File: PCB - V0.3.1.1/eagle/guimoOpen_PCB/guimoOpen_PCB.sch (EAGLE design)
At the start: 8 parts, among them M1 ARDUINO-NANO-3.0, U1 GY-521MPU6050

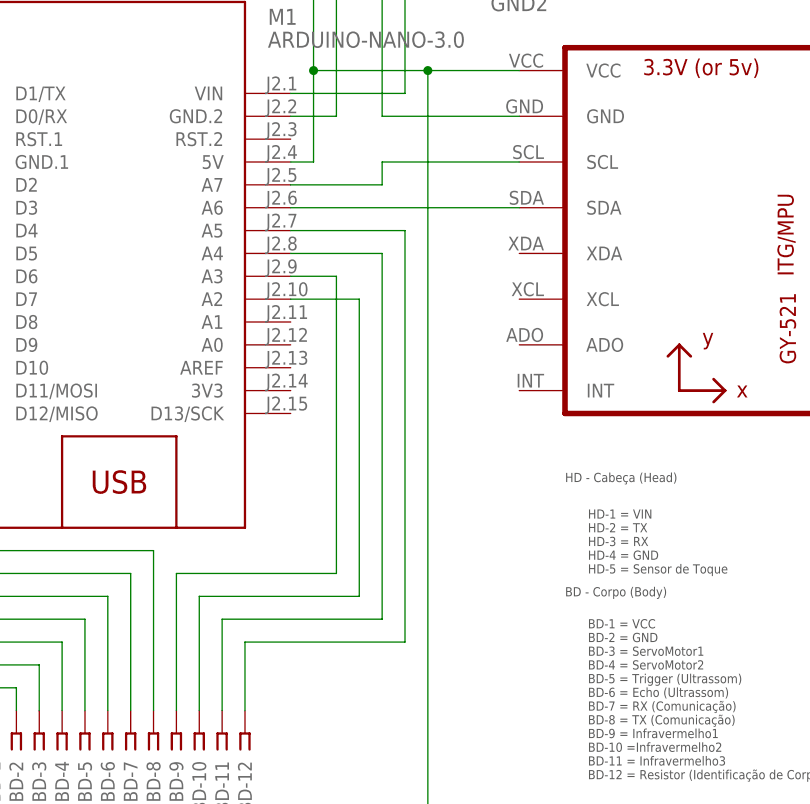
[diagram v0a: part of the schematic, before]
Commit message: Correção do roteamento do acelerômetro. SDA e SCL foram colocadas nas portas A4 e A5
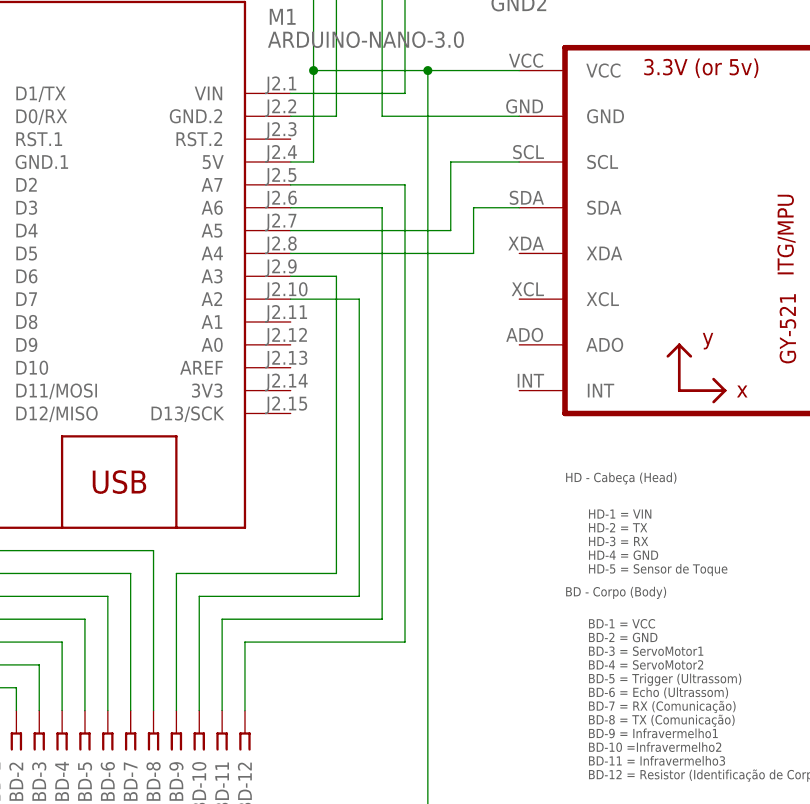
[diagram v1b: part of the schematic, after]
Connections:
- net N$15: now also M1.A7; no longer M1.A5
- net N$16: now also M1.A6; no longer M1.A4
- net N$3: now also M1.A5; no longer M1.A7
- net N$4: now also M1.A4; no longer M1.A6
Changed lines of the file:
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@@
-</segment>
-</net>
-<net name="N$4" class="0">
-<segment>
-<pinref part="U1" gate="G$1" pin="SDA"/>
-<pinref part="M1" gate="G$1" pin="A6"/>
-<wire x1="71.12" y1="88.9" x2="96.52" y2="88.9" width="0.1524" layer="91"/>
 </segment>
 </net>
@@
 <wire x1="66.04" y1="33.02" x2="66.04" y2="40.64" width="0.1524" layer="91"/>
 <wire x1="66.04" y1="40.64" x2="83.82" y2="40.64" width="0.1524" layer="91"/>
-<wire x1="83.82" y1="40.64" x2="83.82" y2="86.36" width="0.1524" layer="91"/>
-<wire x1="83.82" y1="86.36" x2="71.12" y2="86.36" width="0.1524" layer="91"/>
-<pinref part="M1" gate="G$1" pin="A5"/>
+<wire x1="83.82" y1="40.64" x2="83.82" y2="91.44" width="0.1524" layer="91"/>
+<pinref part="M1" gate="G$1" pin="A7"/>
+<wire x1="83.82" y1="91.44" x2="71.12" y2="91.44" width="0.1524" layer="91"/>
 </segment>
 </net>
@@
 <wire x1="63.5" y1="33.02" x2="63.5" y2="43.18" width="0.1524" layer="91"/>
 <wire x1="63.5" y1="43.18" x2="81.28" y2="43.18" width="0.1524" layer="91"/>
-<wire x1="81.28" y1="43.18" x2="81.28" y2="83.82" width="0.1524" layer="91"/>
-<wire x1="81.28" y1="83.82" x2="71.12" y2="83.82" width="0.1524" layer="91"/>
-<pinref part="M1" gate="G$1" pin="A4"/>
+<wire x1="81.28" y1="43.18" x2="81.28" y2="88.9" width="0.1524" layer="91"/>
+<pinref part="M1" gate="G$1" pin="A6"/>
+<wire x1="81.28" y1="88.9" x2="71.12" y2="88.9" width="0.1524" layer="91"/>
 </segment>
 </net>
@@
 <wire x1="78.74" y1="78.74" x2="71.12" y2="78.74" width="0.1524" layer="91"/>
 <pinref part="M1" gate="G$1" pin="A2"/>
-</segment>
-</net>
-<net name="N$3" class="0">
-<segment>
-<pinref part="U1" gate="G$1" pin="SCL"/>
-<wire x1="96.52" y1="93.98" x2="81.28" y2="93.98" width="0.1524" layer="91"/>
-<wire x1="81.28" y1="93.98" x2="81.28" y2="91.44" width="0.1524" layer="91"/>
-<wire x1="81.28" y1="91.44" x2="71.12" y2="91.44" width="0.1524" layer="91"/>
-<pinref part="M1" gate="G$1" pin="A7"/>
 </segment>
 </net>
@@
 </segment>
 </net>
+<net name="N$3" class="0">
+<segment>
+<pinref part="U1" gate="G$1" pin="SCL"/>
+<wire x1="96.52" y1="93.98" x2="88.9" y2="93.98" width="0.1524" layer="91"/>
+<wire x1="88.9" y1="93.98" x2="88.9" y2="86.36" width="0.1524" layer="91"/>
+<pinref part="M1" gate="G$1" pin="A5"/>
+<wire x1="88.9" y1="86.36" x2="71.12" y2="86.36" width="0.1524" layer="91"/>
+</segment>
+</net>
+<net name="N$4" class="0">
+<segment>
+<pinref part="U1" gate="G$1" pin="SDA"/>
+<wire x1="96.52" y1="88.9" x2="91.44" y2="88.9" width="0.1524" layer="91"/>
+<wire x1="91.44" y1="88.9" x2="91.44" y2="83.82" width="0.1524" layer="91"/>
+<pinref part="M1" gate="G$1" pin="A4"/>
+<wire x1="91.44" y1="83.82" x2="71.12" y2="83.82" width="0.1524" layer="91"/>
+</segment>
+</net>
